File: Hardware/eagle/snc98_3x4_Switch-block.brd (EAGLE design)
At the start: 57.1 x 83.8 mm, 52 parts

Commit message: Switch-block changed Rev.02
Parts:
- D1, D10, D11, D12, D13, D14, D15, D2, D29, D3, D4, D5: device BaseApp:SMADIODE -> BaseApp:SMADIODE-WIDE
- H1, H10, H2, H3, H4, H5, H6, H7, H8, H9: value MOUNT-PAD-ROUND2.5 -> MOUNT-PAD-ROUND2.8; device holes:2,5-PAD -> holes:2,8-PAD
- JP1: value M09LOCK-LONGPADS -> (none)
- moved LOGO1 17.8 mm to (39.6, 3.38)
- moved D15 1.27 mm to (45.6, 80.0)
- moved D6 0.63 mm to (45.6, 80.0)
- moved D13 0.25 mm to (11.7, 80.0)
- moved D14 0.25 mm to (11.7, 80.0)
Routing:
- net A2: track 130.2 -> 134.6 mm
- net GND: track 251.4 -> 253.6 mm
- net A3: track 94.8 -> 92.9 mm, vias 3 -> 2
- net N$24: track 44.0 -> 42.7 mm
- net A1: track 128.6 -> 129.3 mm
- net N$2: track 29.9 -> 30.6 mm
- net N$6: track 35.3 -> 35.8 mm
- net N$19: track 30.6 -> 30.5 mm, vias 0 -> 1
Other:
- board text added: "https://oshpark.com/profiles/Jens_G"
- board text added: "snc98 3x4 Switch-block Rev. 0.2"
- board text removed: "goo.gl/5fAHca"
- board text removed: "snc98 3x4 Switch-block Rev. 0.1"

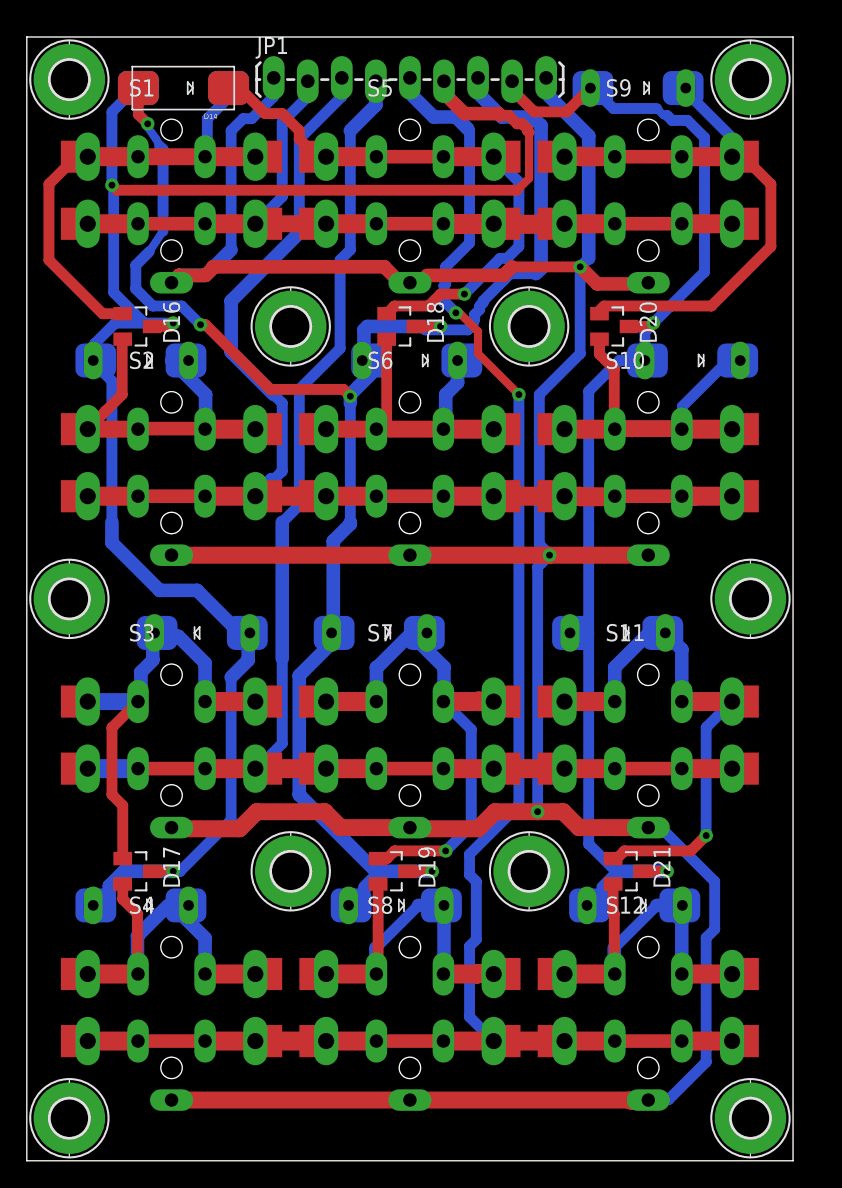
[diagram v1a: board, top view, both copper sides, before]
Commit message: Switch-block Filter added
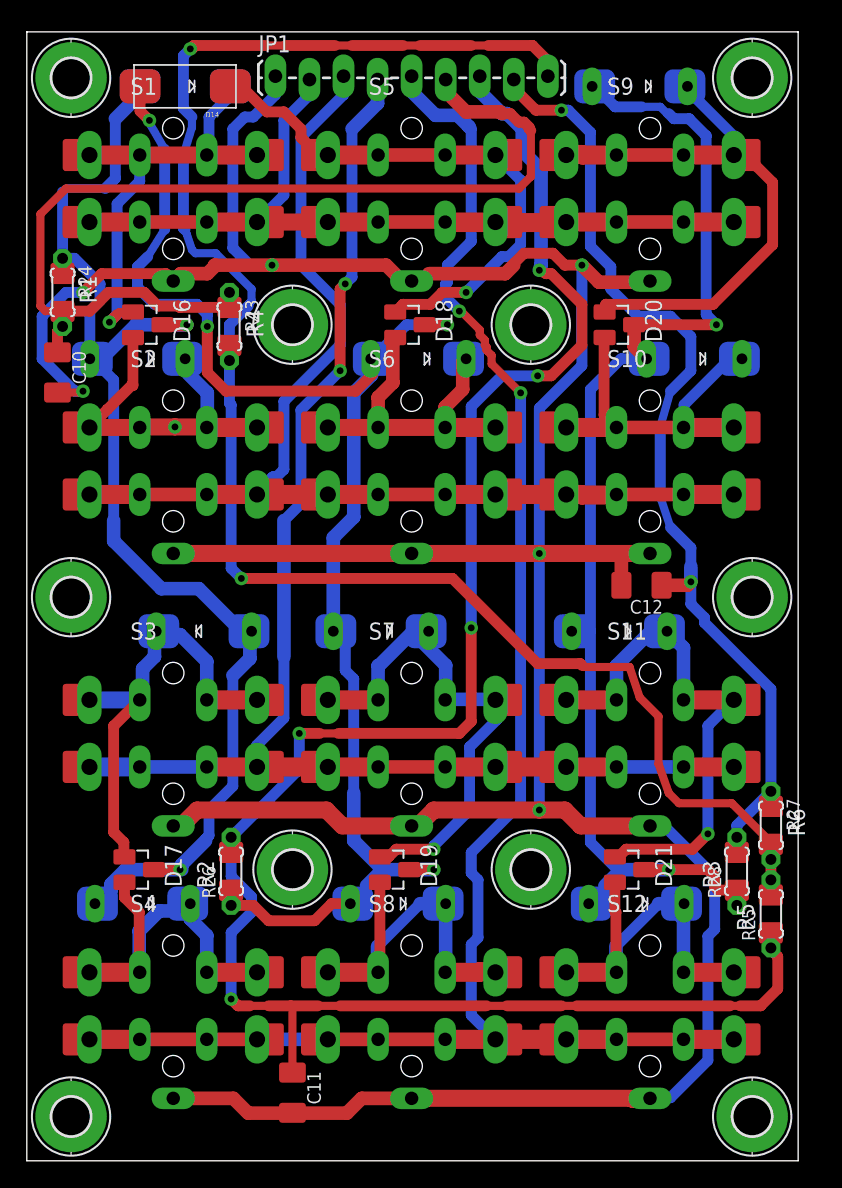
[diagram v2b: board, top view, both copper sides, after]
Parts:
- added C10, C11, C12: 15n, rcl:C1206K
- added R1, R2, R3: 6k8, rcl:R1206
- added R23, R25, R27: 27k, rcl:0204/5
- added R24, R26, R28: 6k8, rcl:0204/5
- added R4, R5, R6: 27k, rcl:R1206
- moved D16 0.77 mm to (9.02, 62.4)
- moved D26 0.65 mm to (29.2, 59.8)
- moved D18 0.65 mm to (28.6, 62.4)
- moved D20 0.40 mm to (44.2, 62.4)
- moved D12 0.28 mm to (8.26, 59.8)
- moved D27 0.28 mm to (8.26, 59.8)
- moved JP1 0.18 mm to (18.5, 80.8)
- moved H1 0.18 mm to (3.30, 80.8)
- moved D10 0.18 mm to (49.8, 59.8)
- moved D11 0.18 mm to (29.2, 59.8)
- moved D7 0.18 mm to (49.8, 59.8)
- moved H4 0.18 mm to (19.8, 62.4)
- moved S10 0.18 mm to (46.5, 52.2)
- moved S6 0.18 mm to (28.7, 52.2)
- moved H8 0.18 mm to (54.1, 80.8)
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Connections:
- new net AREF: JP1.9, R23.2, R25.2, R27.2, R4.2, R5.2, R6.2
- new net A_1: D1.A, D12.A, D13.A, D16.3, D17.3, D23.P$1, D24.P$1, D27.P$1, D29.A, R1.1, R24.1
- new net A_2: D11.A, D14.A, D18.3, D19.3, D2.A, D22.P$1, D25.P$1, D26.P$1, D5.A, R2.1, R26.1
- new net A_3: D10.A, D15.A, D20.3, D21.3, D3.A, D4.A, D6.P$1, D7.P$1, D8.P$1, D9.P$1, R28.1, R3.1
- net A1: now also C10.1, R1.2, R23.1, R24.2, R4.1; no longer D1.A, D12.A, D13.A, D16.3, D17.3, D23.P$1, D24.P$1, D27.P$1, D29.A
- net A2: now also C11.1, R2.2, R25.1, R26.2, R5.1; no longer D11.A, D14.A, D18.3, D19.3, D2.A, D22.P$1, D25.P$1, D26.P$1, D5.A
- net A3: now also C12.1, R27.1, R28.2, R3.2, R6.1; no longer D10.A, D15.A, D20.3, D21.3, D3.A, D4.A, D6.P$1, D7.P$1, D8.P$1, D9.P$1
- net GND: now also C10.2, C11.2, C12.2; no longer JP1.9
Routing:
- net AREF: track 0.00 -> 129.5 mm, vias 0 -> 2
- net A_2: track 0.00 -> 112.1 mm, vias 0 -> 4
- net A_1: track 0.00 -> 98.9 mm, vias 0 -> 2
- net A_3: track 0.00 -> 93.5 mm, vias 0 -> 2
- net A1: track 129.3 -> 76.7 mm, vias 3 -> 0
- net A3: track 92.9 -> 74.4 mm
- net A2: track 134.6 -> 147.0 mm
- net GND: track 253.6 -> 259.3 mm, vias 3 -> 6
- net N$28: track 43.5 -> 40.3 mm
- net C4: track 131.4 -> 133.7 mm
- net N$25: track 27.8 -> 29.1 mm
- net N$30: track 29.7 -> 30.6 mm
- net N$19: track 30.5 -> 29.7 mm
- net C2: track 88.8 -> 88.0 mm
- net N$24: track 42.7 -> 42.2 mm
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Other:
- board size 57.1 x 83.8 mm -> 57.5 x 84.2 mm
- board text added: "snc98 3x4 Switch-block Rev. 0.3"
- board text removed: "snc98 3x4 Switch-block Rev. 0.2"

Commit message: New Picture "Switch mechanical"
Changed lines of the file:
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@@
 <setting verticaltext="up"/>
 </settings>
-<grid distance="5" unitdist="mil" unit="mil" style="dots" multiple="1" display="yes" altdistance="0.005" altunitdist="inch" altunit="inch"/>
+<grid distance="5" unitdist="mil" unit="mm" style="dots" multiple="1" display="yes" altdistance="0.005" altunitdist="inch" altunit="inch"/>
 <layers>
 <layer number="1" name="Top" color="4" fill="1" visible="yes" active="yes"/>
@@
 <layer number="21" name="tPlace" color="16" fill="1" visible="yes" active="yes"/>
 <layer number="22" name="bPlace" color="14" fill="1" visible="yes" active="yes"/>
-<layer number="23" name="tOrigins" color="15" fill="1" visible="no" active="yes"/>
-<layer number="24" name="bOrigins" color="15" fill="1" visible="no" active="yes"/>
-<layer number="25" name="tNames" color="7" fill="1" visible="yes" active="yes"/>
-<layer number="26" name="bNames" color="7" fill="1" visible="yes" active="yes"/>
+<layer number="23" name="tOrigins" color="15" fill="1" visible="yes" active="yes"/>
+<layer number="24" name="bOrigins" color="15" fill="1" visible="yes" active="yes"/>
+<layer number="25" name="tNames" color="7" fill="1" visible="no" active="yes"/>
+<layer number="26" name="bNames" color="7" fill="1" visible="no" active="yes"/>
 <layer number="27" name="tValues" color="7" fill="1" visible="no" active="yes"/>
 <layer number="28" name="bValues" color="7" fill="1" visible="no" active="yes"/>
@@
 <layer number="45" name="Holes" color="7" fill="1" visible="yes" active="yes"/>
 <layer number="46" name="Milling" color="3" fill="1" visible="no" active="yes"/>
-<layer number="47" name="Measures" color="7" fill="1" visible="no" active="yes"/>
-<layer number="48" name="Document" color="7" fill="1" visible="yes" active="yes"/>
+<layer number="47" name="Measures" color="7" fill="1" visible="yes" active="yes"/>
+<layer number="48" name="Document" color="7" fill="1" visible="no" active="yes"/>
 <layer number="49" name="Reference" color="7" fill="1" visible="no" active="yes"/>
 <layer number="50" name="dxf" color="7" fill="1" visible="no" active="yes"/>
@@
 <text x="2.667" y="23.622" size="1.27" layer="22" ratio="16" rot="MR270" align="center">source</text>
 <text x="28.448" y="1.905" size="1.27" layer="22" ratio="16" rot="MR0" align="center">https://oshpark.com/profiles/Jens_G</text>
-<dimension x1="0" y1="-3.81" x2="57.15" y2="-3.81" x3="28.575" y3="-3.81" textsize="1.778" textratio="15" layer="47" dtype="radius"/>
-<dimension x1="-3.81" y1="0" x2="-3.81" y2="83.82" x3="-3.81" y3="41.91" textsize="1.778" textratio="15" layer="47" dtype="radius"/>
 <wire x1="0" y1="84.201" x2="57.531" y2="84.201" width="0" layer="20"/>
 <wire x1="57.531" y1="84.201" x2="57.531" y2="0" width="0" layer="20"/>
@@
 <wire x1="46.5455" y1="80.5815" x2="46.5455" y2="80.137" width="0.127" layer="21"/>
 <wire x1="46.5455" y1="80.137" x2="46.5455" y2="79.6925" width="0.127" layer="21"/>
+<dimension x1="10.922" y1="31.877" x2="10.922" y2="52.197" x3="-1.905" y3="42.037" textsize="1.778" textratio="15" layer="47"/>
+<dimension x1="0" y1="0" x2="0" y2="84.201" x3="-6.477" y3="42.1005" textsize="1.778" textratio="15" layer="47"/>
+<dimension x1="0" y1="0" x2="57.531" y2="0" x3="28.7655" y3="-10.668" textsize="1.778" textratio="15" layer="47"/>
+<dimension x1="10.922" y1="11.557" x2="28.702" y2="11.557" x3="19.812" y3="-4.445" textsize="1.778" textratio="15" layer="47"/>
 </plain>
 <attributes>
@@
 <wire x1="48.006" y1="62.992" x2="49.53" y2="61.468" width="0.8128" layer="16"/>
 <wire x1="49.53" y1="61.468" x2="49.53" y2="58.928" width="0.8128" layer="16"/>
-<wire x1="49.53" y1="58.928" x2="48.006" y2="57.404" width="0.8128" layer="16"/>
-<wire x1="48.006" y1="57.404" x2="47.244" y2="54.737" width="0.6096" layer="16"/>
+<wire x1="49.53" y1="58.928" x2="48.133" y2="57.531" width="0.8128" layer="16"/>
+<wire x1="48.133" y1="57.531" x2="47.244" y2="54.737" width="0.6096" layer="16"/>
 <wire x1="47.244" y1="54.737" x2="47.244" y2="49.53" width="0.8128" layer="16"/>
 <wire x1="47.244" y1="49.53" x2="48.006" y2="47.244" width="0.6096" layer="16"/>
@@
 <wire x1="36.957" y1="76.962" x2="36.957" y2="75.311" width="1.016" layer="16"/>
 <wire x1="36.957" y1="75.311" x2="38.354" y2="73.914" width="1.016" layer="16"/>
-<wire x1="38.354" y1="73.914" x2="38.354" y2="66.802" width="1.016" layer="16"/>
-<wire x1="38.354" y1="66.802" x2="38.227" y2="66.421" width="1.016" layer="16"/>
-<via x="38.227" y="66.421" extent="1-16" drill="0.508"/>
-<wire x1="38.227" y1="66.421" x2="38.735" y2="66.167" width="0.8128" layer="1"/>
+<wire x1="38.354" y1="73.914" x2="38.354" y2="66.294" width="1.016" layer="16"/>
+<via x="38.354" y="66.294" extent="1-16" drill="0.508"/>
+<wire x1="38.354" y1="66.294" x2="38.735" y2="66.167" width="0.8128" layer="1"/>
 <wire x1="38.735" y1="66.167" x2="39.116" y2="66.167" width="0.8128" layer="1"/>
 <wire x1="39.116" y1="66.167" x2="41.402" y2="63.881" width="0.8128" layer="1"/>
@@
 <wire x1="14.097" y1="67.691" x2="12.573" y2="67.691" width="0.6096" layer="16"/>
 <wire x1="12.573" y1="67.691" x2="12.319" y2="67.945" width="0.6096" layer="16"/>
-<wire x1="12.319" y1="67.945" x2="11.938" y2="69.088" width="0.6096" layer="16"/>
 <wire x1="11.684" y1="82.423" x2="12.192" y2="82.931" width="0.8128" layer="16"/>
 <via x="12.192" y="82.931" extent="1-16" drill="0.508"/>
@@
 <wire x1="38.989" y1="81.915" x2="38.989" y2="81.026" width="0.8128" layer="1"/>
 <wire x1="38.989" y1="81.026" x2="38.862" y2="80.899" width="0.8128" layer="1"/>
-<wire x1="11.684" y1="69.85" x2="11.684" y2="69.723" width="0.6096" layer="16"/>
-<wire x1="11.684" y1="69.723" x2="11.7978625" y2="69.43834375" width="0.6096" layer="16"/>
-<wire x1="11.7978625" y1="69.43834375" x2="11.938" y2="69.088" width="0.6096" layer="16"/>
+<wire x1="11.684" y1="69.85" x2="11.684" y2="69.80620625" width="0.6096" layer="16"/>
 <wire x1="37.719" y1="83.185" x2="38.989" y2="81.915" width="0.8128" layer="1"/>
 <wire x1="37.719" y1="83.185" x2="34.417" y2="83.185" width="0.8128" layer="1"/>
@@
 <wire x1="11.811" y1="75.438" x2="11.811" y2="75.311" width="0.6096" layer="16"/>
 <wire x1="11.811" y1="75.311" x2="11.684" y2="75.184" width="0.6096" layer="16"/>
-<wire x1="11.684" y1="75.184" x2="11.684" y2="69.55220625" width="0.8128" layer="16"/>
-<wire x1="11.684" y1="69.55220625" x2="11.7978625" y2="69.43834375" width="0.8128" layer="16"/>
+<wire x1="11.684" y1="75.184" x2="11.684" y2="69.80620625" width="0.8128" layer="16"/>
 <wire x1="55.499" y1="20.955" x2="55.499" y2="22.479" width="0.8128" layer="1"/>
 <wire x1="55.499" y1="23.597" x2="55.499" y2="22.479" width="0.8128" layer="1"/>
@@
 <via x="16.002" y="43.434" extent="1-16" drill="0.508"/>
 <wire x1="16.002" y1="43.434" x2="31.75" y2="43.434" width="0.8128" layer="1"/>
+<wire x1="12.319" y1="67.945" x2="11.684" y2="69.80620625" width="0.6096" layer="16"/>
 </signal>
 <signal name="A_1">

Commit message: PCB_Display_make
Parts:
- moved D16 0.25 mm to (8.76, 62.4)
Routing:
- net N$19: track 29.7 -> 28.6 mm

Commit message: Debug_Level 13:  - Protokoll Statepoint
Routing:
- net AREF: track 129.1 -> 128.6 mm
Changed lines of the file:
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@@
 <setting verticaltext="up"/>
 </settings>
-<grid distance="0.05" unitdist="inch" unit="inch" style="dots" multiple="1" display="yes" altdistance="0.005" altunitdist="inch" altunit="inch"/>
+<grid distance="10" unitdist="mil" unit="mil" style="dots" multiple="1" display="yes" altdistance="0.005" altunitdist="inch" altunit="inch"/>
 <layers>
 <layer number="1" name="Top" color="4" fill="1" visible="yes" active="yes"/>
@@
 <layer number="45" name="Holes" color="7" fill="1" visible="yes" active="yes"/>
 <layer number="46" name="Milling" color="3" fill="1" visible="no" active="yes"/>
-<layer number="47" name="Measures" color="7" fill="1" visible="yes" active="yes"/>
+<layer number="47" name="Measures" color="7" fill="1" visible="no" active="yes"/>
 <layer number="48" name="Document" color="7" fill="1" visible="no" active="yes"/>
 <layer number="49" name="Reference" color="7" fill="1" visible="no" active="yes"/>
@@
 </class>
 </classes>
-<designrules name="SparkFun_Iteadstudio_10mil *">
+<designrules name="OSHPark-8mil-2layer">
 <description language="en">&lt;b&gt;EAGLE Design Rules&lt;/b&gt;
 &lt;p&gt;
@@
 <param name="mtCopper" value="0.035mm 0.035mm 0.035mm 0.035mm 0.035mm 0.035mm 0.035mm 0.035mm 0.035mm 0.035mm 0.035mm 0.035mm 0.035mm 0.035mm 0.035mm 0.035mm"/>
 <param name="mtIsolate" value="1.5mm 0.15mm 0.2mm 0.15mm 0.2mm 0.15mm 0.2mm 0.15mm 0.2mm 0.15mm 0.2mm 0.15mm 0.2mm 0.15mm 0.2mm"/>
-<param name="mdWireWire" value="12mil"/>
-<param name="mdWirePad" value="12mil"/>
-<param name="mdWireVia" value="12mil"/>
-<param name="mdPadPad" value="12mil"/>
-<param name="mdPadVia" value="12mil"/>
-<param name="mdViaVia" value="12mil"/>
-<param name="mdSmdPad" value="12mil"/>
-<param name="mdSmdVia" value="12mil"/>
-<param name="mdSmdSmd" value="12mil"/>
+<param name="mdWireWire" value="8mil"/>
+<param name="mdWirePad" value="8mil"/>
+<param name="mdWireVia" value="8mil"/>
+<param name="mdPadPad" value="8mil"/>
+<param name="mdPadVia" value="8mil"/>
+<param name="mdViaVia" value="8mil"/>
+<param name="mdSmdPad" value="8mil"/>
+<param name="mdSmdVia" value="8mil"/>
+<param name="mdSmdSmd" value="8mil"/>
 <param name="mdViaViaSameLayer" value="8mil"/>
 <param name="mnLayersViaInSmd" value="2"/>
-<param name="mdCopperDimension" value="0.5mm"/>
+<param name="mdCopperDimension" value="8mil"/>
 <param name="mdDrill" value="8mil"/>
 <param name="mdSmdStop" value="0mil"/>
 <param name="msWidth" value="10mil"/>
-<param name="msDrill" value="20mil"/>
+<param name="msDrill" value="15mil"/>
 <param name="msMicroVia" value="9.99mm"/>
 <param name="msBlindViaRatio" value="0.5"/>
@@
 <param name="mlMinCreamFrame" value="0mil"/>
 <param name="mlMaxCreamFrame" value="0mil"/>
-<param name="mlViaStopLimit" value="25mil"/>
+<param name="mlViaStopLimit" value="20mil"/>
 <param name="srRoundness" value="0"/>
 <param name="srMinRoundness" value="0mil"/>
@@
 <wire x1="14.097" y1="67.691" x2="12.573" y2="67.691" width="0.6096" layer="16"/>
 <wire x1="12.573" y1="67.691" x2="12.319" y2="67.945" width="0.6096" layer="16"/>
-<wire x1="11.684" y1="82.423" x2="12.192" y2="82.931" width="0.8128" layer="16"/>
-<via x="12.192" y="82.931" extent="1-16" drill="0.508"/>
-<wire x1="12.192" y1="82.931" x2="12.319" y2="82.931" width="0.8128" layer="1"/>
+<via x="11.684" y="82.169" extent="1-16" drill="0.508"/>
 <wire x1="12.319" y1="82.931" x2="12.573" y2="83.185" width="0.8128" layer="1"/>
 <wire x1="38.989" y1="81.915" x2="38.989" y2="81.026" width="0.8128" layer="1"/>
@@
 <wire x1="22.987" y1="83.185" x2="19.304" y2="83.185" width="0.8128" layer="1"/>
 <wire x1="19.304" y1="83.185" x2="17.78" y2="83.185" width="0.6096" layer="1"/>
-<wire x1="17.78" y1="83.185" x2="12.446" y2="83.185" width="0.8128" layer="1"/>
-<wire x1="12.446" y1="83.185" x2="12.192" y2="82.931" width="0.8128" layer="1"/>
-<wire x1="11.684" y1="82.423" x2="11.684" y2="78.486" width="0.8128" layer="16"/>
+<wire x1="17.78" y1="83.185" x2="12.573" y2="83.185" width="0.8128" layer="1"/>
+<wire x1="11.684" y1="82.169" x2="11.684" y2="78.486" width="0.8128" layer="16"/>
 <wire x1="11.684" y1="78.486" x2="12.319" y2="77.851" width="0.8128" layer="16"/>
 <wire x1="12.319" y1="77.851" x2="12.319" y2="77.089" width="0.6096" layer="16"/>
@@
 <wire x1="16.002" y1="43.434" x2="31.75" y2="43.434" width="0.8128" layer="1"/>
 <wire x1="12.319" y1="67.945" x2="11.684" y2="69.80620625" width="0.6096" layer="16"/>
+<wire x1="12.319" y1="82.931" x2="12.319" y2="82.804" width="0.8128" layer="1"/>
+<wire x1="12.319" y1="82.804" x2="11.684" y2="82.169" width="0.8128" layer="1"/>
 </signal>
 <signal name="A_1">

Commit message: Debuglevel 13 - Protokoll Statepoint
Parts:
- moved H8 1.44 mm to (53.1, 79.8)
- moved D15 1.14 mm to (44.7, 79.6)
- moved D6 1.14 mm to (44.7, 79.6)
- moved H9 1.14 mm to (53.1, 41.5)
- moved H1 1.02 mm to (3.30, 79.8)
- moved H10 1.02 mm to (53.1, 3.30)
- moved JP1 0.72 mm to (18.0, 80.3)
- moved C12 0.72 mm to (45.3, 42.4)
- moved H4 0.72 mm to (19.3, 61.8)
- moved S10 0.72 mm to (46.0, 51.7)
- moved S6 0.72 mm to (28.2, 51.7)
- moved D12 0.72 mm to (7.75, 59.3)
- moved D24 0.72 mm to (12.7, 39.0)
- moved D27 0.72 mm to (7.75, 59.3)
- moved D29 0.72 mm to (12.7, 39.0)
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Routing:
- net N$16: track 45.0 -> 45.9 mm
- net A3: track 74.3 -> 75.0 mm
- net N$24: track 42.1 -> 41.6 mm
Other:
- board size 57.5 x 84.2 mm -> 56.4 x 83.2 mm
